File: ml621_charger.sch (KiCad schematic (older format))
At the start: 9 parts, among them J1 Conn_01x05

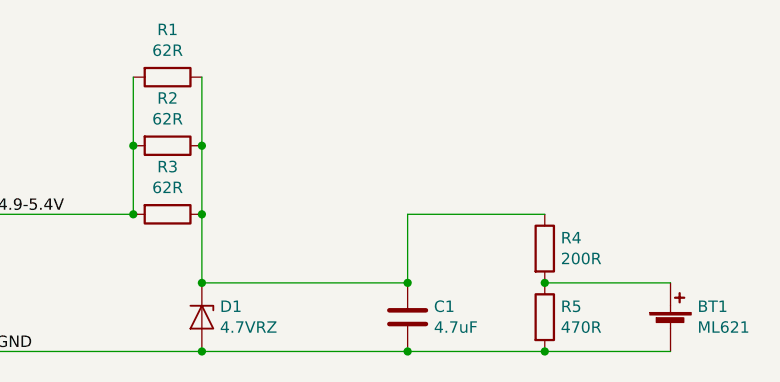
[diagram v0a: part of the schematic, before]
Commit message: Add schottkey diode to ensure reverse protection
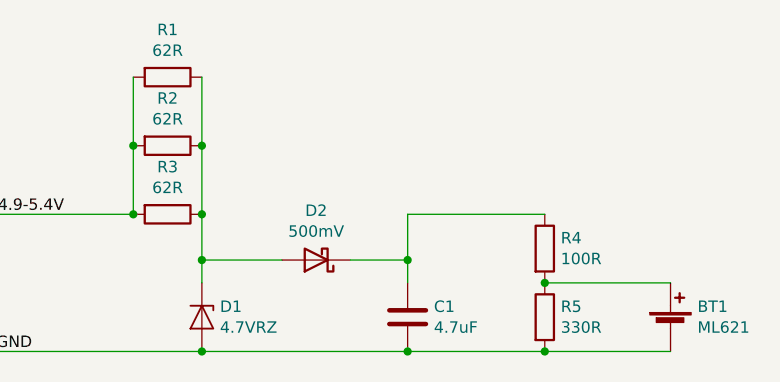
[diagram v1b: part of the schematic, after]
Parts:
- added D2: 500mV, Diode_SMD:D_SOD-523, symbol Device:D_Schottky
- R4: value 200R -> 100R
- R5: value 470R -> 330R
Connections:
- net at D1.1 (K), R1.1, R2.1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: now also D2.2 (A); no longer C1.1, R4.1
- new net: C1.1, D2.1 (K), R4.1
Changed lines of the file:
@@
 Connection ~ 3650 3000
 Wire Wire Line
-	3650 3300 3650 3000
+	3650 3300 3650 3200
 $Comp
 L Device:R R3
@@
 	5150 3300 5700 3300
 Wire Wire Line
-	4550 3000 4550 3300
-Connection ~ 4550 3300
+	4550 3000 4550 3200
 $Comp
 L Device:R R5
@@
 P 5150 3450
 F 0 "R5" H 5220 3496 50  0000 L CNN
-F 1 "470R" H 5220 3405 50  0000 L CNN
+F 1 "330R" H 5220 3405 50  0000 L CNN
 F 2 "Resistor_SMD:R_0805_2012Metric" V 5080 3450 50  0001 C CNN
 F 3 "~" H 5150 3450 50  0001 C CNN
@@
 P 5150 3150
 F 0 "R4" H 5220 3196 50  0000 L CNN
-F 1 "200R" H 5220 3105 50  0000 L CNN
+F 1 "100R" H 5220 3105 50  0000 L CNN
 F 2 "Resistor_SMD:R_0805_2012Metric" V 5080 3150 50  0001 C CNN
 F 3 "~" H 5150 3150 50  0001 C CNN
@@
 	3350 2400 3350 2700
 Wire Wire Line
-	3650 3300 4550 3300
-Connection ~ 3650 3300
-Wire Wire Line
 	3650 3600 4550 3600
 Connection ~ 3650 3600
@@
 	4550 3600 5150 3600
 Connection ~ 4550 3600
+$Comp
+L Device:D_Schottky D2
+U 1 1 5D897290
+P 4150 3200
+F 0 "D2" H 4150 2984 50  0000 C CNN
+F 1 "500mV" H 4150 3075 50  0000 C CNN
+F 2 "Diode_SMD:D_SOD-523" H 4150 3200 50  0001 C CNN
+F 3 "~" H 4150 3200 50  0001 C CNN
+	1    4150 3200
+	-1   0    0    1
+$EndComp
+Wire Wire Line
+	4000 3200 3650 3200
+Connection ~ 3650 3200
+Wire Wire Line
+	3650 3200 3650 3000
+Wire Wire Line
+	4300 3200 4550 3200
+Connection ~ 4550 3200
+Wire Wire Line
+	4550 3200 4550 3300
 $EndSCHEMATC

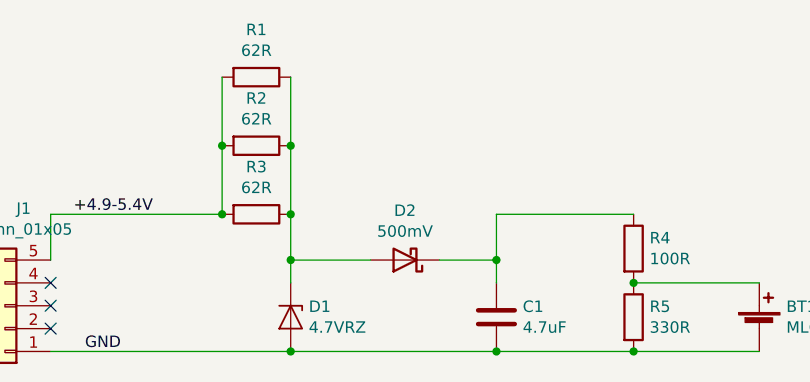
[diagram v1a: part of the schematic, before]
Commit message: Fix schottkey diode rating
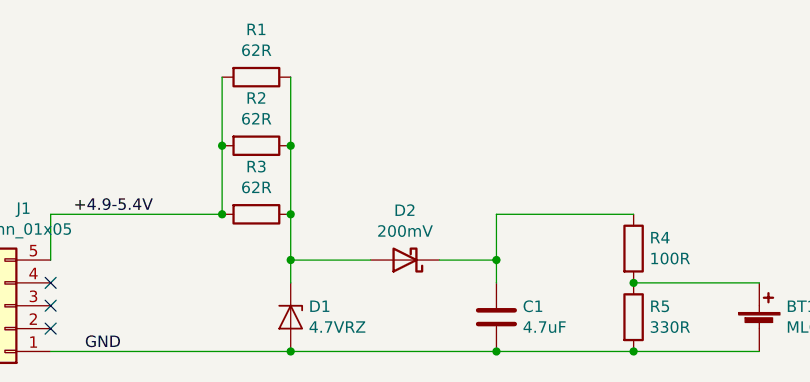
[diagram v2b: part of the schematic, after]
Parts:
- D2: value 500mV -> 200mV
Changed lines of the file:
@@
 P 4150 3200
 F 0 "D2" H 4150 2984 50  0000 C CNN
-F 1 "500mV" H 4150 3075 50  0000 C CNN
+F 1 "200mV" H 4150 3075 50  0000 C CNN
 F 2 "Diode_SMD:D_SOD-523" H 4150 3200 50  0001 C CNN
 F 3 "~" H 4150 3200 50  0001 C CNN

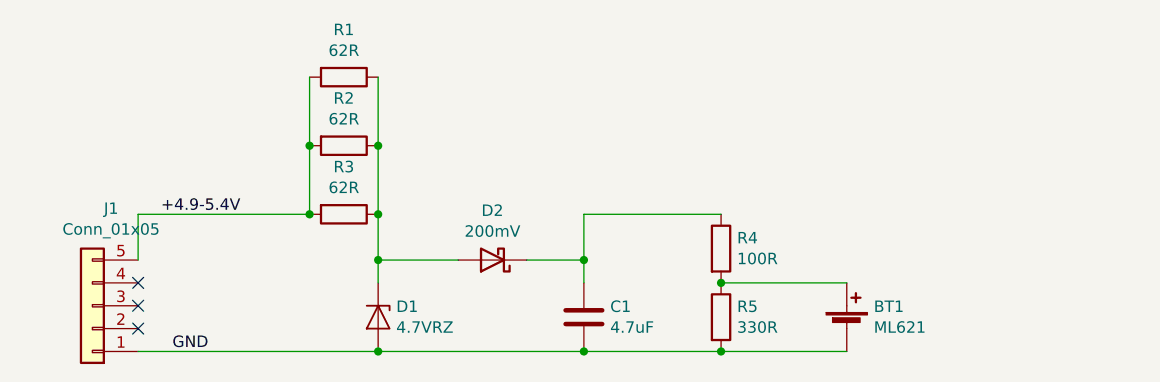
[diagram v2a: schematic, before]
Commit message: Put USB connector directly on; add indicator LEDs
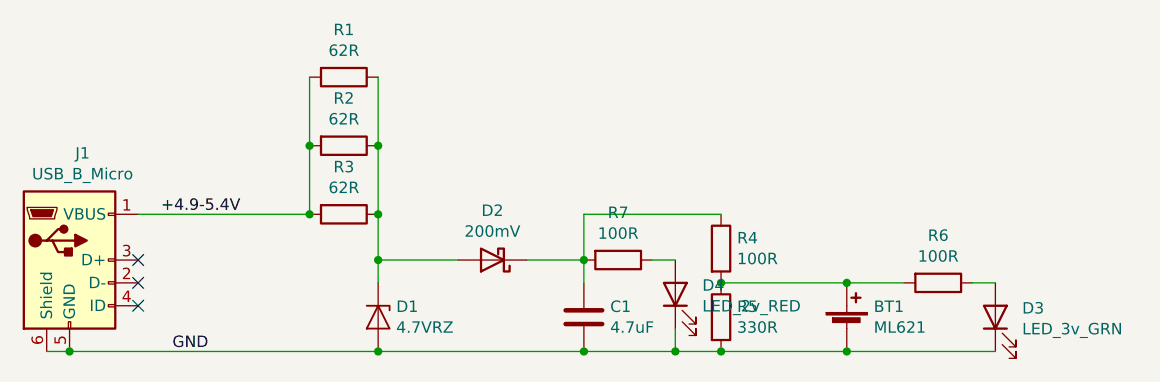
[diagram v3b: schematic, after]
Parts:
- removed J1: Conn_01x05, Connector_PinHeader_2.54mm:PinHeader_1x05_P2.54mm_Vertical, symbol Connector_Generic:Conn_01x05
- added D3: LED_3v_GRN, LED_SMD:LED_0805_2012Metric, symbol Device:LED
- added D4: LED_2v_RED, LED_SMD:LED_0805_2012Metric, symbol Device:LED
- added J1: USB_B_Micro, digikey-footprints:USB_Micro_B_Female_10118194-0001LF, symbol Connector:USB_B_Micro
- added R6, R7: 100R, Resistor_SMD:R_0805_2012Metric, symbol Device:R
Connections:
- net +4.9-5.4V: now also J1.1 (VBUS)
- net GND: now also D3.1 (K), D4.1 (K), J1.5 (GND), J1.6 (Shield)
- net at BT1.1 (+), R4.2, R5.1: now also R6.2
- net at C1.1, D2.1 (K), R4.1: now also R7.2
- new net: D3.2 (A), R6.1
- new net: D4.2 (A), R7.1
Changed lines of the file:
@@
 Wire Wire Line
 	2600 3000 3350 3000
-Wire Wire Line
-	2600 3200 2600 3000
-NoConn ~ 2600 3500
-NoConn ~ 2600 3400
-NoConn ~ 2600 3300
-$Comp
-L Connector_Generic:Conn_01x05 J1
-U 1 1 5D7C896E
-P 2400 3400
-F 0 "J1" H 2318 2975 50  0000 C CNN
-F 1 "Conn_01x05" H 2318 3066 50  0000 C CNN
-F 2 "Connector_PinHeader_2.54mm:PinHeader_1x05_P2.54mm_Vertical" H 2400 3400 50  0001 C CNN
-F 3 "~" H 2400 3400 50  0001 C CNN
-	1    2400 3400
-	-1   0    0    1
-$EndComp
-Wire Wire Line
-	2600 3600 3650 3600
 Connection ~ 3350 3000
 Text Label 2700 3000 0    50   ~ 0
@@
 Wire Wire Line
 	3650 3600 4550 3600
-Connection ~ 3650 3600
 Wire Wire Line
 	4550 3000 5150 3000
 Wire Wire Line
-	4550 3600 5150 3600
+	4550 3600 4950 3600
 Connection ~ 4550 3600
 $Comp
@@
 Wire Wire Line
 	4550 3200 4550 3300
+$Comp
+L Connector:USB_B_Micro J1
+U 1 1 5DF6F8CD
+P 2300 3200
+F 0 "J1" H 2357 3667 50  0000 C CNN
+F 1 "USB_B_Micro" H 2357 3576 50  0000 C CNN
+F 2 "digikey-footprints:USB_Micro_B_Female_10118194-0001LF" H 2450 3150 50  0001 C CNN
+F 3 "~" H 2450 3150 50  0001 C CNN
+	1    2300 3200
+	1    0    0    -1
+$EndComp
+Wire Wire Line
+	2300 3600 3650 3600
+Connection ~ 3650 3600
+Wire Wire Line
+	2300 3600 2200 3600
+Connection ~ 2300 3600
+NoConn ~ 2600 3400
+NoConn ~ 2600 3300
+NoConn ~ 2600 3200
+$Comp
+L Device:LED D3
+U 1 1 5DF6FA9D
+P 6350 3450
+F 0 "D3" V 6389 3333 50  0000 R CNN
+F 1 "LED_3v_GRN" V 6298 3333 50  0000 R CNN
+F 2 "LED_SMD:LED_0805_2012Metric" H 6350 3450 50  0001 C CNN
+F 3 "~" H 6350 3450 50  0001 C CNN
+	1    6350 3450
+	0    -1   -1   0
+$EndComp
+$Comp
+L Device:R R6
+U 1 1 5DF700E4
+P 6100 3300
+F 0 "R6" V 5893 3300 50  0000 C CNN
+F 1 "100R" V 5984 3300 50  0000 C CNN
+F 2 "Resistor_SMD:R_0805_2012Metric" V 6030 3300 50  0001 C CNN
+F 3 "~" H 6100 3300 50  0001 C CNN
+	1    6100 3300
+	0    1    1    0
+$EndComp
+Wire Wire Line
+	5700 3300 5950 3300
+Connection ~ 5700 3300
+Wire Wire Line
+	6250 3300 6350 3300
+Wire Wire Line
+	6350 3600 5700 3600
+Connection ~ 5700 3600
+$Comp
+L Device:LED D4
+U 1 1 5DF73081
+P 4950 3350
+F 0 "D4" V 4989 3232 50  0000 R CNN
+F 1 "LED_2v_RED" V 4898 3232 50  0000 R CNN
+F 2 "LED_SMD:LED_0805_2012Metric" H 4950 3350 50  0001 C CNN
+F 3 "~" H 4950 3350 50  0001 C CNN
+	1    4950 3350
+	0    -1   -1   0
+$EndComp
+$Comp
+L Device:R R7
+U 1 1 5DF73087
+P 4700 3200
+F 0 "R7" V 4493 3200 50  0000 C CNN
+F 1 "100R" V 4584 3200 50  0000 C CNN
+F 2 "Resistor_SMD:R_0805_2012Metric" V 4630 3200 50  0001 C CNN
+F 3 "~" H 4700 3200 50  0001 C CNN
+	1    4700 3200
+	0    1    1    0
+$EndComp
+Wire Wire Line
+	4850 3200 4950 3200
+Wire Wire Line
+	4950 3500 4950 3600
+Connection ~ 4950 3600
+Wire Wire Line
+	4950 3600 5150 3600
 $EndSCHEMATC

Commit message: Change around some values
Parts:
- R1, R2: value 62R -> 10R
- R7: value 100R -> 330R
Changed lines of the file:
@@
 P 3500 2700
 F 0 "R2" V 3293 2700 50  0000 C CNN
-F 1 "62R" V 3384 2700 50  0000 C CNN
+F 1 "10R" V 3384 2700 50  0000 C CNN
 F 2 "Resistor_SMD:R_0805_2012Metric" V 3430 2700 50  0001 C CNN
 F 3 "~" H 3500 2700 50  0001 C CNN
@@
 P 3500 2400
 F 0 "R1" V 3293 2400 50  0000 C CNN
-F 1 "62R" V 3384 2400 50  0000 C CNN
+F 1 "10R" V 3384 2400 50  0000 C CNN
 F 2 "Resistor_SMD:R_0805_2012Metric" V 3430 2400 50  0001 C CNN
 F 3 "~" H 3500 2400 50  0001 C CNN
@@
 P 4700 3200
 F 0 "R7" V 4493 3200 50  0000 C CNN
-F 1 "100R" V 4584 3200 50  0000 C CNN
+F 1 "330R" V 4584 3200 50  0000 C CNN
 F 2 "Resistor_SMD:R_0805_2012Metric" V 4630 3200 50  0001 C CNN
 F 3 "~" H 4700 3200 50  0001 C CNN

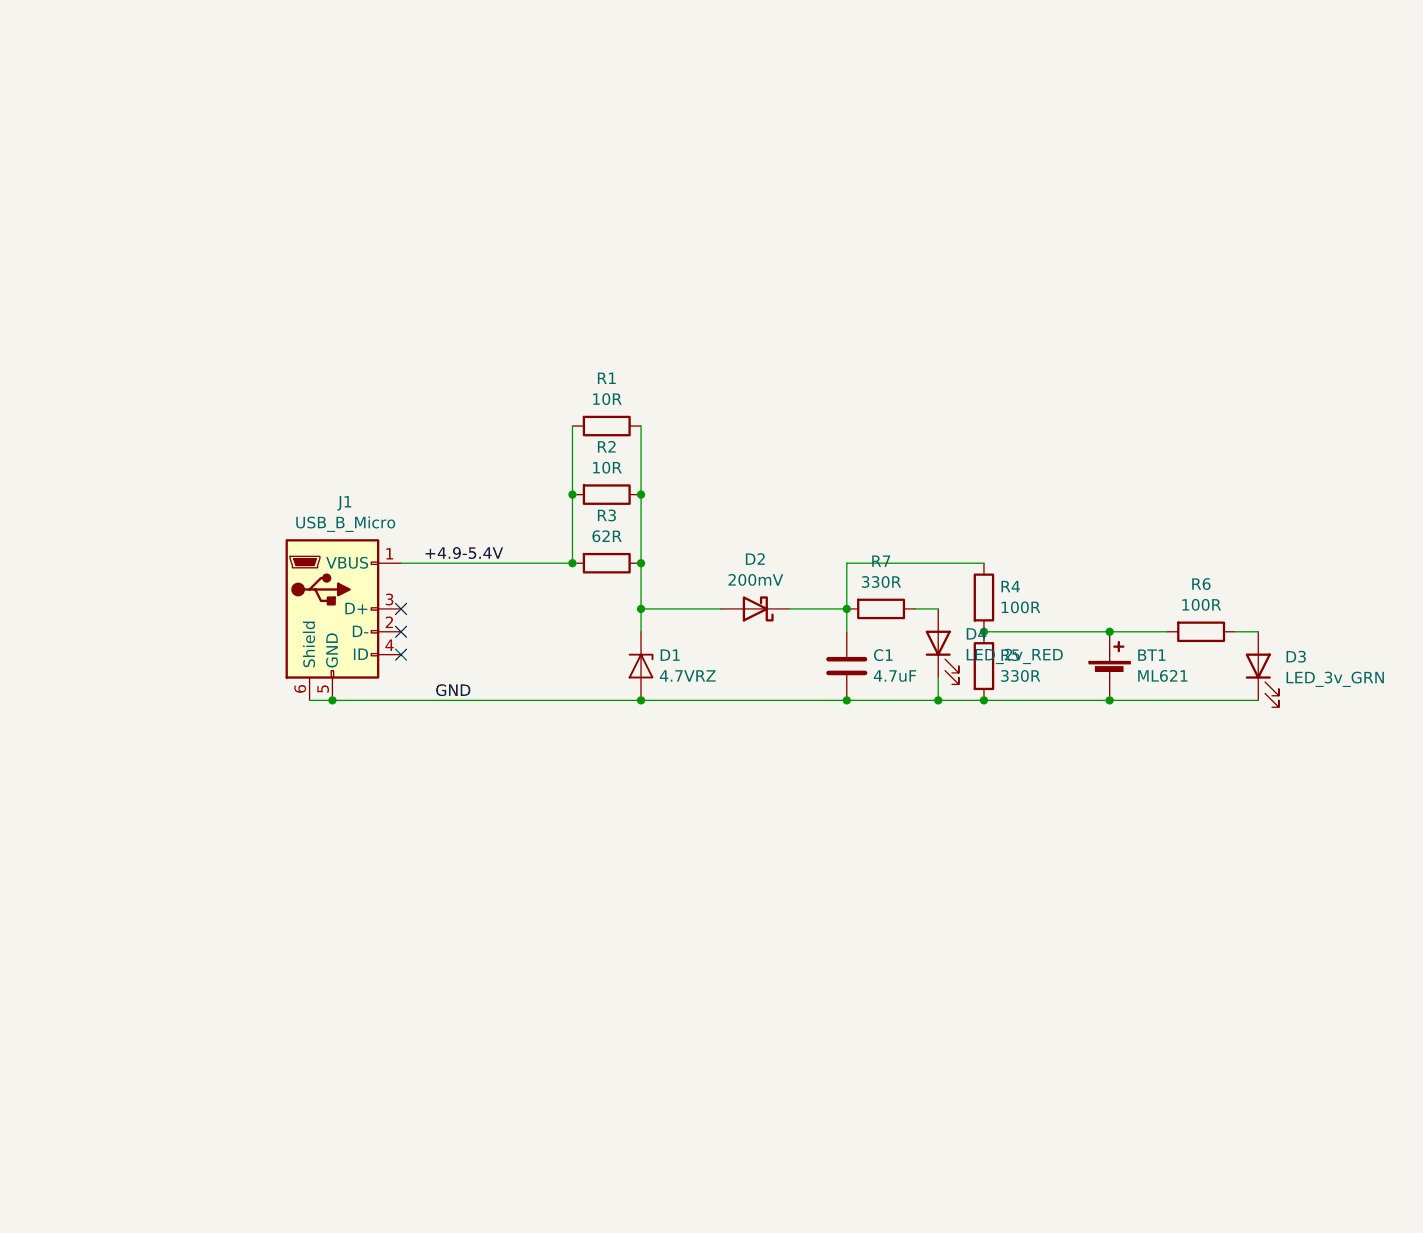
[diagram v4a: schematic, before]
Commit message: V3 with a microcontroller
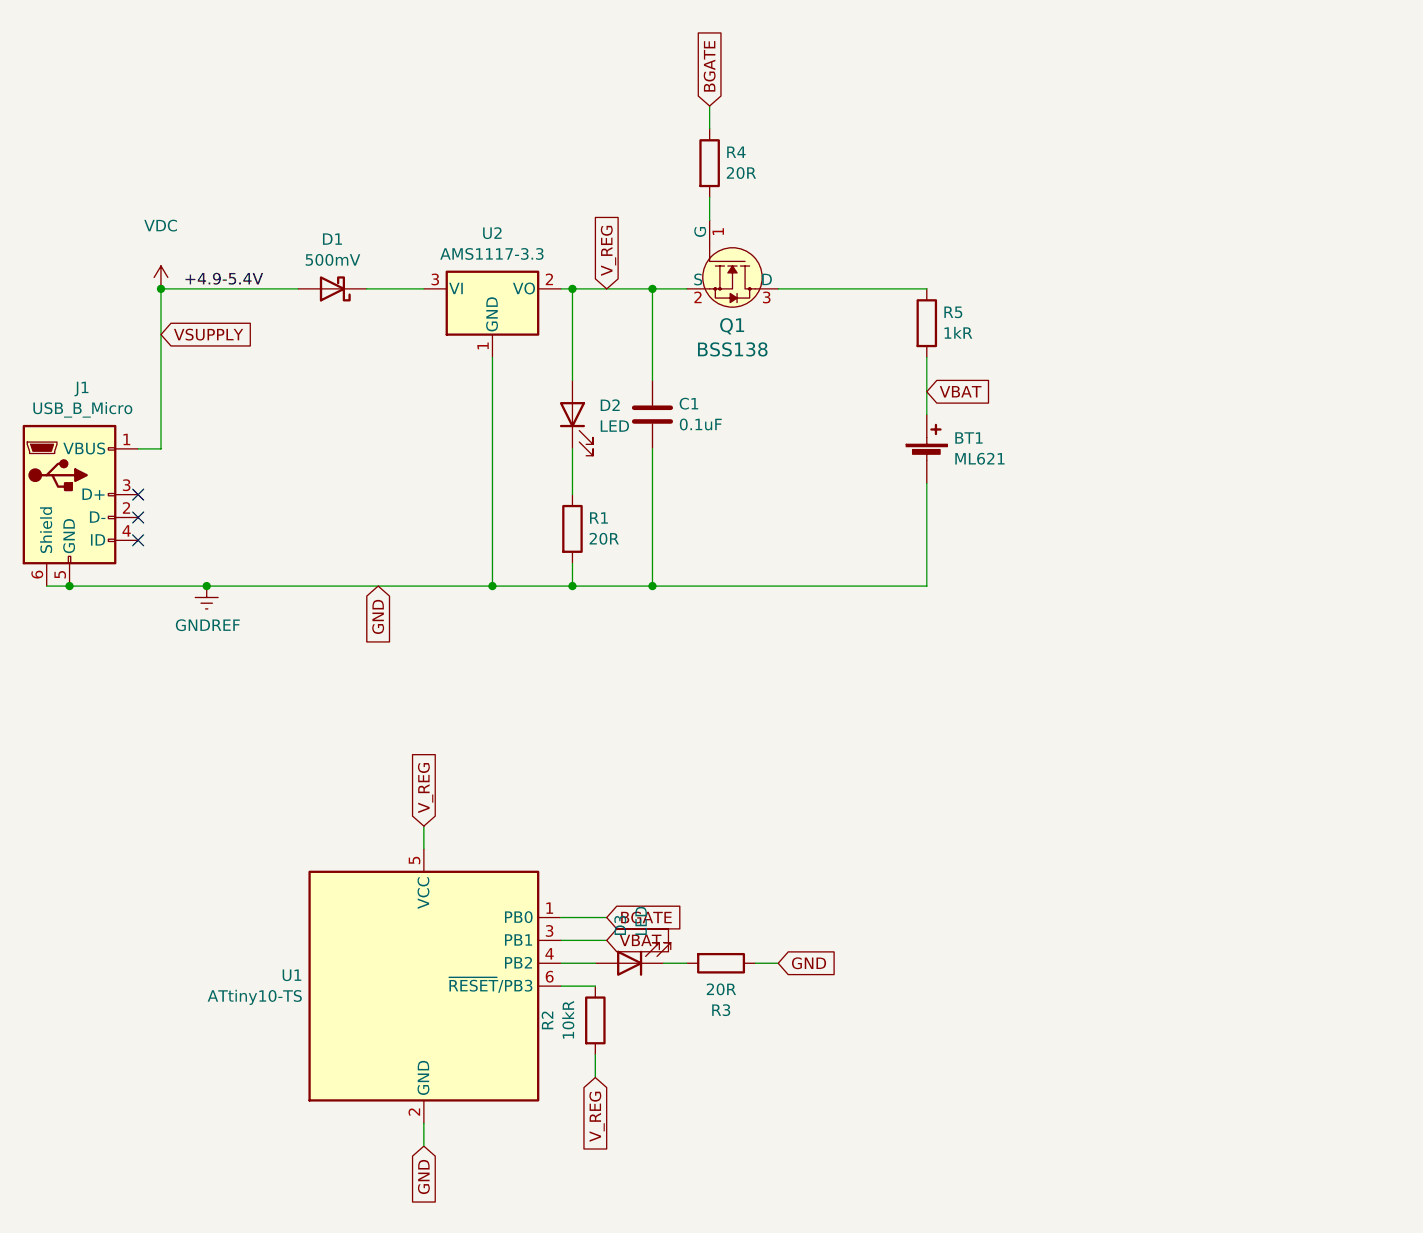
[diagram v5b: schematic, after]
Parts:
- removed D1: 4.7VRZ, Diode_SMD:D_SOD-323, symbol Device:D_Zener
- removed D2: 200mV, Diode_SMD:D_SOD-523, symbol Device:D_Schottky
- removed D4: LED_2v_RED, LED_SMD:LED_0805_2012Metric, symbol Device:LED
- removed R6: 100R, Resistor_SMD:R_0805_2012Metric, symbol Device:R
- removed R7: 330R, Resistor_SMD:R_0805_2012Metric, symbol Device:R
- added D1: 500mV, Diode_SMD:D_SOD-523, symbol Device:D_Schottky
- added D2: LED, LED_SMD:LED_0805_2012Metric, symbol Device:LED
- added Q1: BSS138, digikey-footprints:SOT-23-3, symbol dk_Transistors-FETs-MOSFETs-Single:BSS138
- added U1: ATtiny10-TS, Package_TO_SOT_SMD:SOT-23-6, symbol MCU_Microchip_ATtiny:ATtiny10-TS
- added U2: AMS1117-3.3, Package_TO_SOT_SMD:SOT-23, symbol Regulator_Linear:AMS1117-3.3
- C1: value 4.7uF -> 0.1uF; footprint Capacitor_SMD:C_0805_2012Metric -> Capacitor_SMD:C_0603_1608Metric
- D3: value LED_3v_GRN -> LED
- R1: value 10R -> 20R
- R2: value 10R -> 10kR
- R3: value 62R -> 20R
- R4: value 100R -> 20R
- R5: value 330R -> 1kR
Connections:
- net BGATE: now reaches R4.1
- net BGATE: now also U1.1 (PB0); no longer C1.1
- net at D3.2 (A): now also U1.4 (PB2)
- removed net +4.9-5.4V: J1.1 (VBUS), R1.2, R2.2, R3.2
- net GND renamed GNDREF
- net GNDREF: now also R1.2, R3.1, U1.2 (GND), U2.1 (GND); no longer D3.1 (K), R5.2
- new net: D1.1 (K), U2.3 (VI)
- new net: D2.1 (K), R1.1
- new net: R2.1, U1.6 (~RESET~/PB3)
- new net: Q1.1 (G), R4.2
- new net: Q1.3 (D), R5.1
- new net: D3.1 (K), R3.2
- new net VBAT: BT1.1 (+), R5.2, U1.3 (PB1)
- new net VDC: D1.2 (A), J1.1 (VBUS)
- new net V_REG: C1.1, D2.2 (A), Q1.2 (S), R2.2, U1.5 (VCC), U2.2 (VO)
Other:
- moved on the sheet: BT1, J1
